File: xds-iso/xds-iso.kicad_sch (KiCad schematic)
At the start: 108 parts, among them J1 USB4085, J2 TGT_JTAG, J3 IF_JTAG, J4 Conn_01x02_Male, SW2 EVQPUD, U1 MCP1703A-3002_SOT223, U2 MSP432E401Y, U3 ISOW7741, U4 ISOW7741, U5 TPD4E004DRYR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

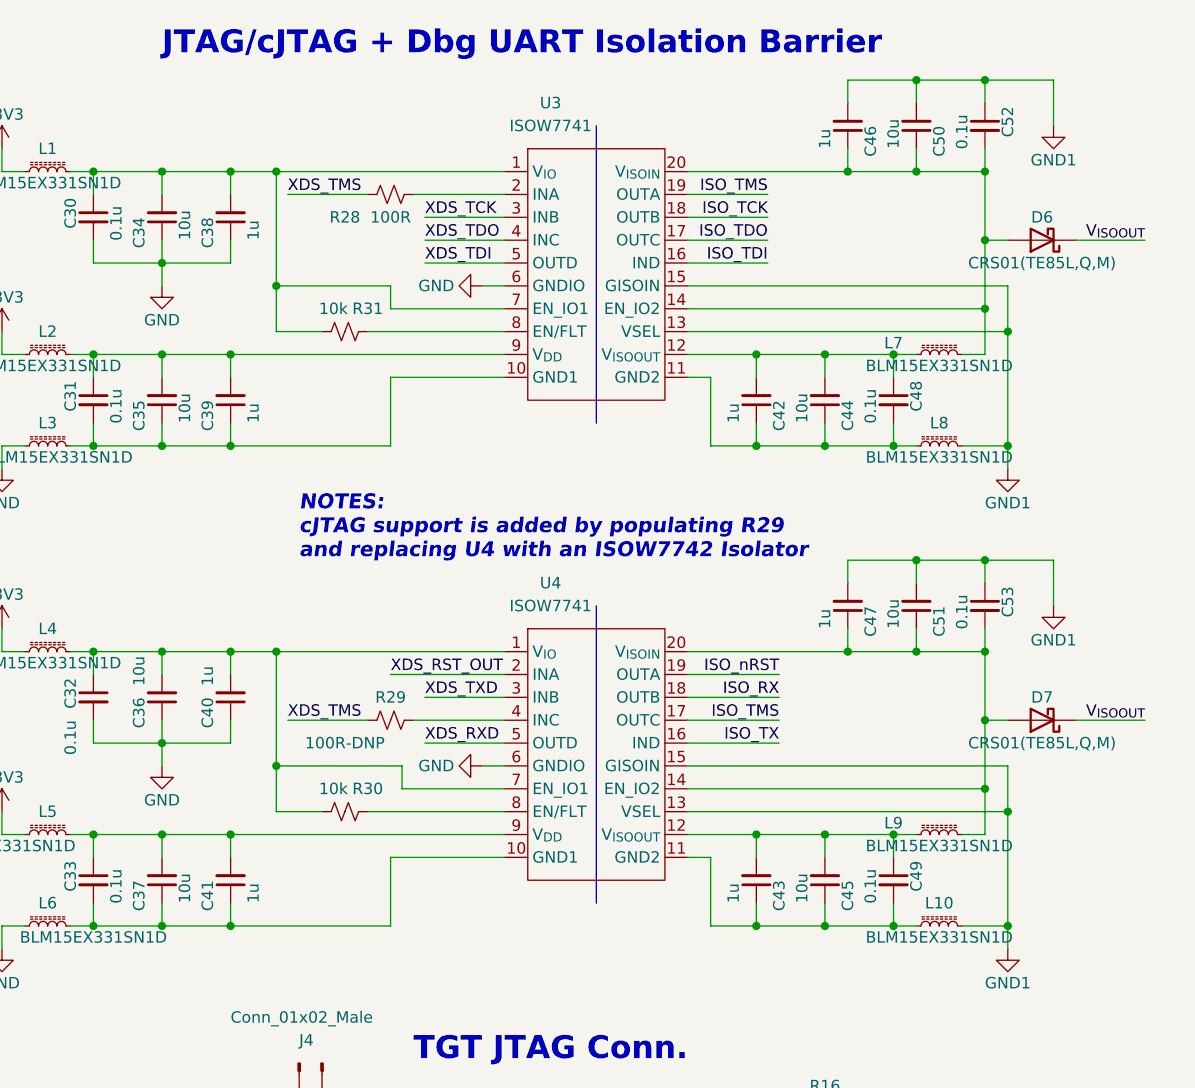
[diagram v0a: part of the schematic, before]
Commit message: R02 updates supporting cJTAG and SWD
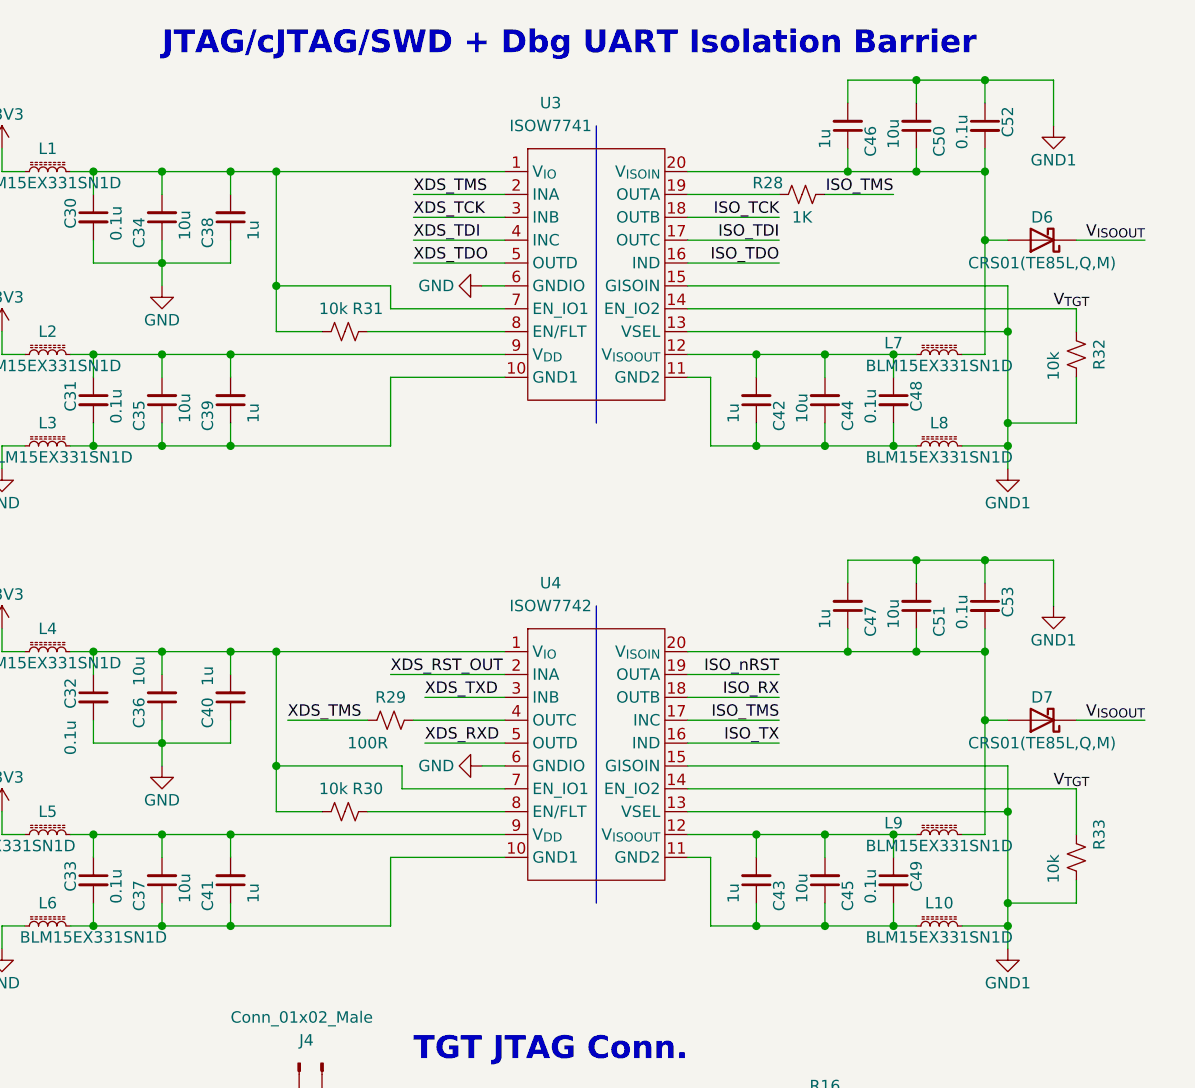
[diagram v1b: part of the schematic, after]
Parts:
- removed U4: ISOW7741, xds-iso:SOIC-20, symbol xds-iso:ISOW7741
- added R32, R33: 10k, Resistor_SMD:R_0402_1005Metric, symbol Device:R_Small_US
- added U4: ISOW7742, xds-iso:SOIC-20, symbol xds-iso:ISOW7742
- R28: value 100R -> 1K
- R29: value 100R-DNP -> 100R
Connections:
- net GND: now also U4.6 (GNDIO)
- net GND1: now also R32.2, R33.2, U4.13 (VSEL), U4.15 (GISOIN)
- net ISO_RX: now also U4.18 (OUTB)
- net ISO_TDI: now also U3.17 (OUTC); no longer U3.16 (IND)
- net ISO_TDO: now also U3.16 (IND); no longer U3.17 (OUTC)
- net ISO_TMS: now also R28.2, U4.17 (INC); no longer U3.19 (OUTA)
- net ISO_TX: now also U4.16 (IND)
- net ISO_nRST: now also U4.19 (OUTA)
- net V_{TGT}: now also U3.14 (EN_IO2), R32.1, R33.1, U4.14 (EN_IO2)
- net XDS_RST_OUT: now also U4.2 (INA)
- net XDS_RXD: now also U4.5 (OUTD)
- net XDS_TDI: now also U3.4 (INC); no longer U3.5 (OUTD)
- net XDS_TDO: now also U3.5 (OUTD); no longer U3.4 (INC)
- net XDS_TMS: now also U3.2 (INA); no longer R28.1
- net XDS_TXD: now also U4.3 (INB)
- net at C33.1, C37.2, C41.2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: now also U4.9 (V_{DD})
- net at C32.1, C36.2, C40.2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: now also U4.1 (V_{IO}), U4.7 (EN_IO1)
- net at C43.1, C45.1, C49.2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: now also U4.11 (GND2)
- net at C43.2, C45.2, C49.1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: now also U4.12 (V_{ISOOUT})
- net at C46.1, C50.1, C52.2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: no longer U3.14 (EN_IO2)
- net at C33.2, C37.1, C41.1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: now also U4.10 (GND1)
- net at C47.1, C51.1, C53.2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: now also U4.20 (V_{ISOIN})
- net at R29.2: now also U4.4 (OUTC)
- net at R30.1: now also U4.8 (EN/FLT)
- new net: R28.1, U3.19 (OUTA)
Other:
- note added: "JTAG/cJTAG/SWD + Dbg UART Isolation Barrier"
- note removed: "JTAG/cJTAG + Dbg UART Isolation Barrier"
- note removed: "NOTES: cJTAG support is added by populating R29 and replacing U4 with an ISOW7742 Isolator"
- title: XDS Isolated JTAG/cJTAG Debugger -> XDS Isolated JTAG/cJTAG/SWD Debugger

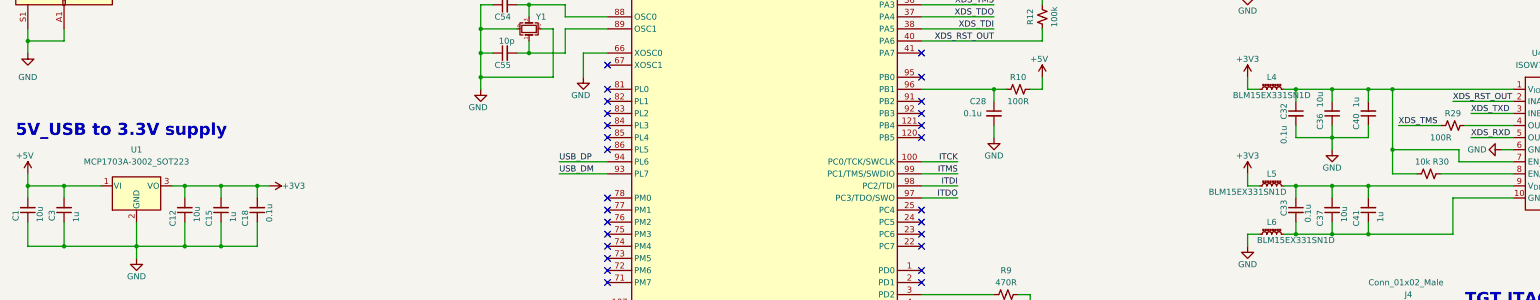
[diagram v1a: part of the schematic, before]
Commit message: Changed TMS series resistor to 1k
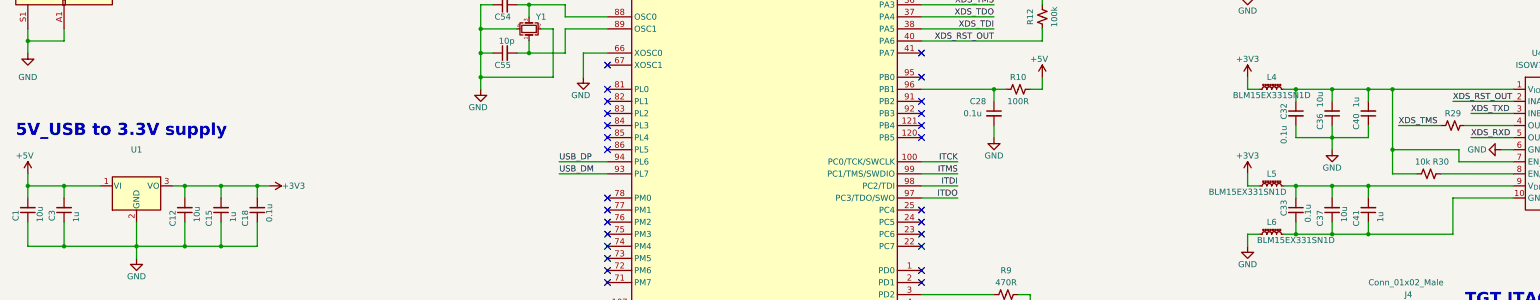
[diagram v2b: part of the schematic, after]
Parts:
- R29: value 100R -> (none); footprint Resistor_SMD:R_0402_1005Metric -> (none)
- U1: value MCP1703A-3002_SOT223 -> (none); footprint Package_TO_SOT_SMD:SOT-223-3_TabPin2 -> (none)
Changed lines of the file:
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@@
     (in_bom yes) (on_board yes) (fields_autoplaced)
     (property "Reference" "U1" (id 0) (at 55.88 101.6 0))
-    (property "Value" "MCP1703A-3002_SOT223" (id 1) (at 55.88 104.14 0))
-    (property "Footprint" "Package_TO_SOT_SMD:SOT-223-3_TabPin2" (id 2) (at 55.88 104.14 0)
+    (property "Value" "" (id 1) (at 55.88 104.14 0))
+    (property "Footprint" "" (id 2) (at 55.88 104.14 0)
       (effects (font (size 1.27 1.27)) hide)
     )
@@
     (in_bom yes) (on_board yes)
     (property "Reference" "R29" (id 0) (at 332.74 93.98 90))
-    (property "Value" "100R" (id 1) (at 330.2 99.06 90))
-    (property "Footprint" "Resistor_SMD:R_0402_1005Metric" (id 2) (at 332.74 96.52 0)
+    (property "Value" "" (id 1) (at 330.2 99.06 90))
+    (property "Footprint" "" (id 2) (at 332.74 96.52 0)
       (effects (font (size 1.27 1.27)) hide)
     )
@@
     )
     (path "/d16f2faa-881f-401e-851c-4725777d416e"
-      (reference "R29") (unit 1) (value "100R") (footprint "Resistor_SMD:R_0402_1005Metric")
+      (reference "R29") (unit 1) (value "1k") (footprint "Resistor_SMD:R_0402_1005Metric")
     )
     (path "/a6ae6ce8-c863-49e5-a79c-9f6fda71b784"
@@
     )
     (path "/39dfe24b-4a86-4229-8b5c-2960b9bae886"
-      (reference "U1") (unit 1) (value "MCP1703A-3002_SOT223") (footprint "Package_TO_SOT_SMD:SOT-223-3_TabPin2")
+      (reference "U1") (unit 1) (value "AP7361EA-33E-13") (footprint "Package_TO_SOT_SMD:SOT-223-3_TabPin2")
     )
     (path "/d1d62dd8-ab18-4589-8a16-4840d0e3a2b2"

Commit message: Add images and update README
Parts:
- R29: value (none) -> 1k; footprint (none) -> Resistor_SMD:R_0402_1005Metric
- U1: value (none) -> AP7361EA-33E-13; footprint (none) -> Package_TO_SOT_SMD:SOT-223-3_TabPin2
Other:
- note added: "TGT Prog Conn."
- note removed: "TGT JTAG Conn."
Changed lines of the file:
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@@
     (effects (font (size 1.27 1.27)) (justify left bottom))
   )
-  (text "TGT JTAG Conn." (at 335.28 134.62 0)
+  (text "TGT Prog Conn." (at 335.28 134.62 0)
     (effects (font (size 2.54 2.54) (thickness 0.508) bold) (justify left bottom))
   )
@@
     (in_bom yes) (on_board yes) (fields_autoplaced)
     (property "Reference" "U1" (id 0) (at 55.88 101.6 0))
-    (property "Value" "" (id 1) (at 55.88 104.14 0))
-    (property "Footprint" "" (id 2) (at 55.88 104.14 0)
+    (property "Value" "AP7361EA-33E-13" (id 1) (at 55.88 104.14 0))
+    (property "Footprint" "Package_TO_SOT_SMD:SOT-223-3_TabPin2" (id 2) (at 55.88 104.14 0)
       (effects (font (size 1.27 1.27)) hide)
     )
@@
     (in_bom yes) (on_board yes)
     (property "Reference" "R29" (id 0) (at 332.74 93.98 90))
-    (property "Value" "" (id 1) (at 330.2 99.06 90))
-    (property "Footprint" "" (id 2) (at 332.74 96.52 0)
-      (effects (font (size 1.27 1.27)) hide)
-    )
+    (property "Value" "1k" (id 1) (at 330.2 99.06 90))
+    (property "Footprint" "Resistor_SMD:R_0402_1005Metric" (id 2) (at 332.74 96.52 0)
+      (effects (font (size 1.27 1.27)) hide)
+    )
